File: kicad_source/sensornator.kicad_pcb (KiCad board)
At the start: 2 copper layers, 78 x 53 mm, 63 parts, among them CN1 ARDUINO, CON1 Micro_SDCard, P1 USB_OTG, Q1 2N7002, Q2 2N7002, Q3 BC847, Q4 BC847, Q5 NTR4171P, SW1 TAST_VER, SW2 TAST_VER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

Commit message: added pull up on BOOT
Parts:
- removed G*** (x2): generationmake_logo, labels:generationmake_logo
- added R25: 10k, Resistor_SMD:R_0603_1608Metric, F.Cu at (81.9, 113.5)
- BT1: value Battery -> Keystone 1043
- C9: value 100n -> 10u
- F1: value F_Small -> SF-1206S050
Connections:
- CN1 pad 15: (no net) -> unconnected-(CN1-Pad15)
- CN1 pad 31: (no net) -> unconnected-(CN1-Pad31)
- CON1 pad 1: (no net) -> unconnected-(CON1-Pad1)
- CON1 pad 8: (no net) -> unconnected-(CON1-Pad8)
- P1 pad 4: (no net) -> unconnected-(P1-Pad4)
- P1 pad 6: GND -> unconnected-(P1-Pad6)
- SW3 pad 3: (no net) -> unconnected-(SW3-Pad3)
- U3 pad 4: (no net) -> unconnected-(U3-Pad4)
- U4 pad 1: (no net) -> unconnected-(U4-Pad1)
- U4 pad 10: (no net) -> unconnected-(U4-Pad10)
- U4 pad 11: (no net) -> unconnected-(U4-Pad11)
- U4 pad 12: (no net) -> unconnected-(U4-Pad12)
- U4 pad 14: (no net) -> unconnected-(U4-Pad14)
- U4 pad 16: (no net) -> unconnected-(U4-Pad16)
- U4 pad 17: (no net) -> unconnected-(U4-Pad17)
- U4 pad 2: (no net) -> unconnected-(U4-Pad2)
- U4 pad 20: (no net) -> unconnected-(U4-Pad20)
- U4 pad 21: (no net) -> unconnected-(U4-Pad21)
- U4 pad 22: (no net) -> unconnected-(U4-Pad22)
- U4 pad 23: (no net) -> unconnected-(U4-Pad23)
- U4 pad 27: (no net) -> unconnected-(U4-Pad27)
- U5 pad 17: (no net) -> unconnected-(U5-Pad17)
- U5 pad 18: (no net) -> unconnected-(U5-Pad18)
- U5 pad 19: (no net) -> unconnected-(U5-Pad19)
- U5 pad 20: (no net) -> unconnected-(U5-Pad20)
- U5 pad 21: (no net) -> unconnected-(U5-Pad21)
- U5 pad 22: (no net) -> unconnected-(U5-Pad22)
- U5 pad 32: (no net) -> unconnected-(U5-Pad32)
- U6 pad 1: (no net) -> unconnected-(U6-Pad1)
- U6 pad 2: (no net) -> unconnected-(U6-Pad2)
- U6 pad 3: (no net) -> unconnected-(U6-Pad3)
- U6 pad 7: (no net) -> unconnected-(U6-Pad7)
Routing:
- net unconnected-(P1-Pad6): track 0.00 -> 8.00 mm
- net BOOT: track 42.1 -> 46.5 mm
- net +3V3: track 202.5 -> 205.4 mm
- net unconnected-(CON1-Pad1): track 0.00 -> 1.57 mm
- net (no net): track 1.57 -> 0.00 mm
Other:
- net class ANTENNA removed
- net class Default removed
- board text added: "1.2"
- board text removed: "1.1"

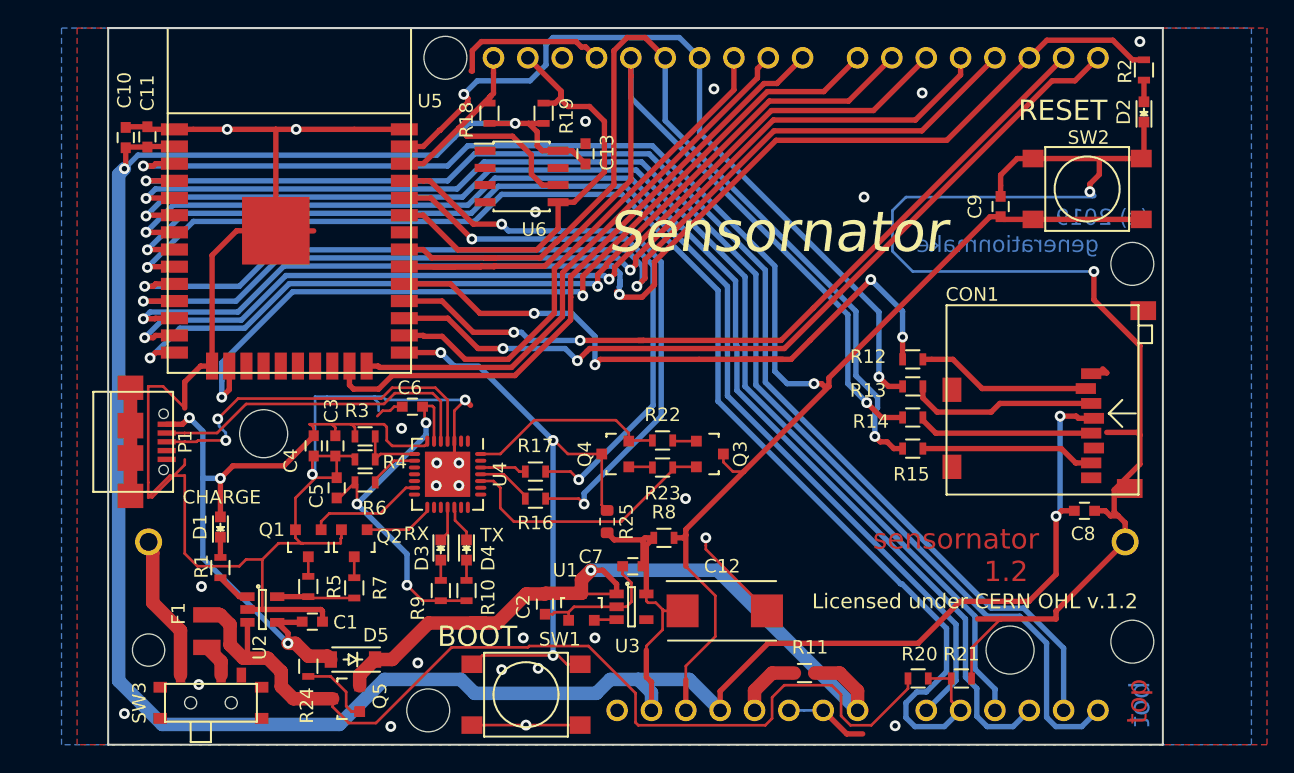
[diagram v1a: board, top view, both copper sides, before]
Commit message: added qwiic connector
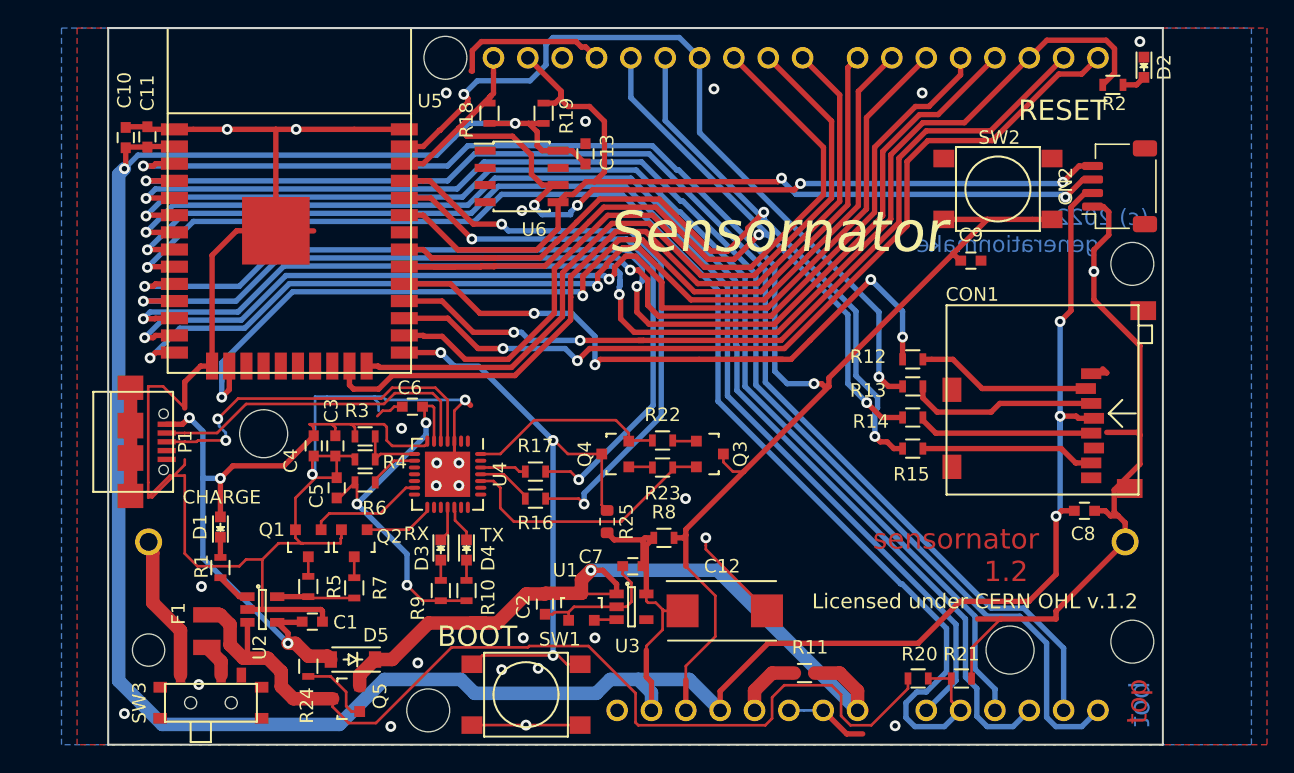
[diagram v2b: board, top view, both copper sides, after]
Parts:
- added CN2: SM04B-SRSS-TB, Connector_JST:JST_SH_SM04B-SRSS-TB_1x04-1MP_P1.00mm_Horizontal, F.Cu at (119.8, 88.7)
- moved SW2 6.60 mm to (110.8, 88.9)
- moved C9 4.57 mm to (108.8, 94.2), turned to 0 degrees
- moved D2 3.30 mm to (121.6, 79.9), turned to -90 degrees
- moved R2 2.55 mm to (119.3, 81.2), turned to 180 degrees
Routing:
- net GND: track 290.7 -> 244.6 mm, vias 29 -> 28
- net /I2C_SCL: track 21.9 -> 67.6 mm, vias 0 -> 4
- net /I2C_SDA: track 32.9 -> 71.0 mm, vias 0 -> 2
- net +3V3: track 205.4 -> 224.1 mm, vias 4 -> 5
- net /SPI_CS_EXT: track 37.7 -> 54.8 mm
- net /ARDUINO_9: track 41.5 -> 57.0 mm
- net /ARDUINO_8: track 47.0 -> 60.3 mm
- net /ARDUINO_7: track 62.5 -> 71.7 mm
- net /ARDUINO_5: track 69.1 -> 77.4 mm
- net /ARDUINO_6: track 66.8 -> 74.9 mm
- net /DAC_2: track 72.0 -> 78.4 mm
- net /DAC_1: track 76.6 -> 82.1 mm
- net /ARDUINO_2: track 89.9 -> 95.0 mm
- net /EXT_RX: track 61.9 -> 64.7 mm
- net /EXT_TX: track 63.3 -> 66.1 mm
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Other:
- board text added: "(c) 2022"
- board text removed: "(c) 2019"

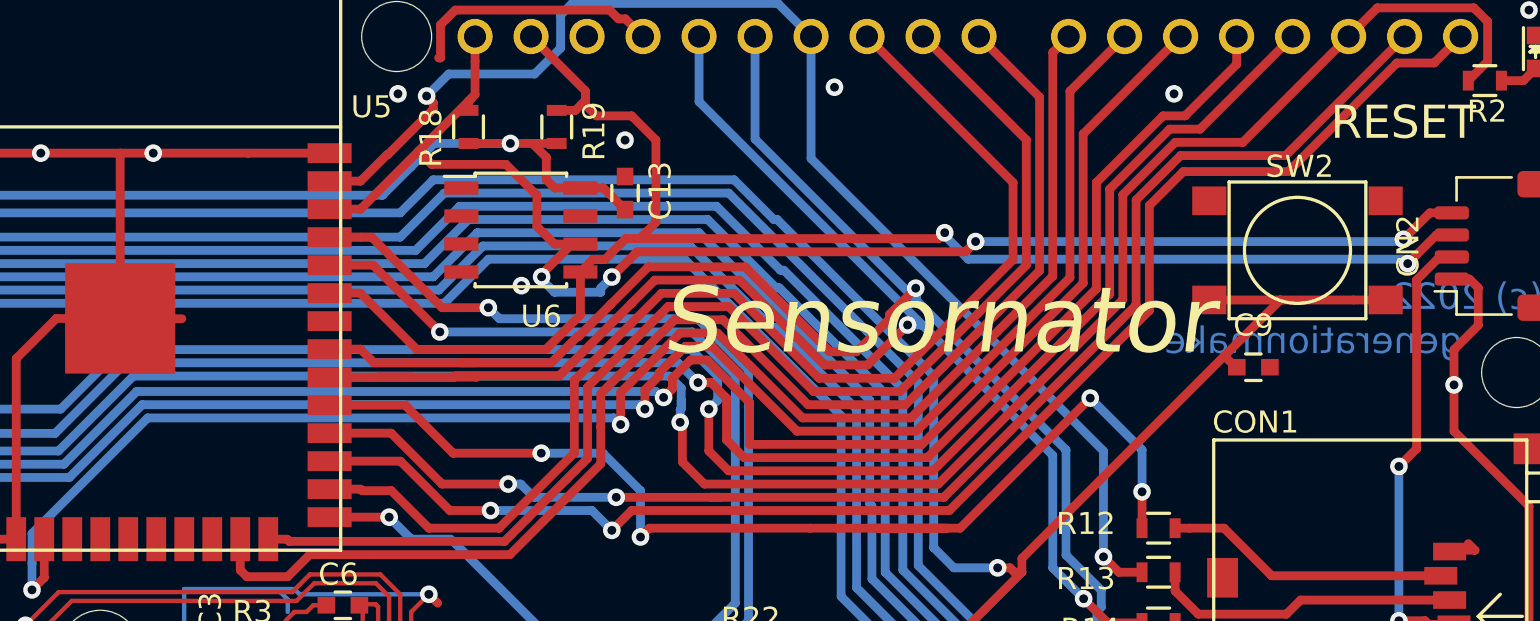
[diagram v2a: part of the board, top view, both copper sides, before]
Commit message: added i2c eeprom
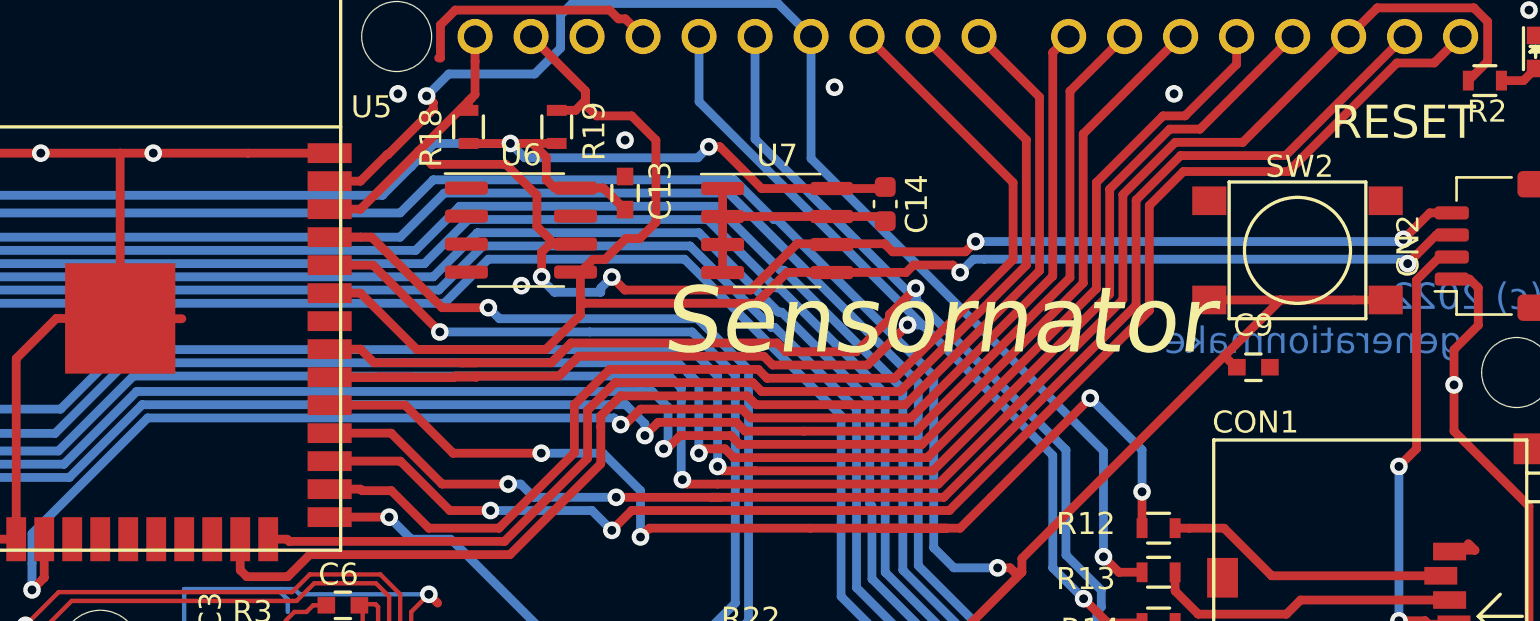
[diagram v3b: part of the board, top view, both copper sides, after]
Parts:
- added C14: 100n, Capacitor_SMD:C_0603_1608Metric, F.Cu at (92.1, 86.8)
- added U7: 24LC64, Package_SO:SOIC-8_3.9x4.9mm_P1.27mm, F.Cu at (87.2, 88.0)
- U6: footprint SOIC:SOIC-8_3.9x4.9mm_Pitch1.27mm -> Package_SO:SOIC-8_3.9x4.9mm_P1.27mm
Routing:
- net +3V3: track 224.1 -> 242.4 mm, vias 5 -> 6
- net GND: track 244.6 -> 255.9 mm
- net /ARDUINO_7: track 71.7 -> 68.0 mm
- net /SPI_CS_EXT: track 54.8 -> 51.3 mm
- net /ARDUINO_9: track 57.0 -> 53.5 mm
- net /ARDUINO_8: track 60.3 -> 56.9 mm
- net /I2C_SDA: track 71.0 -> 74.4 mm
- net /SPI_MISO: track 69.8 -> 67.0 mm
- net /SPI_CLK: track 75.2 -> 72.3 mm
- net /ARDUINO_6: track 74.9 -> 72.8 mm
- net /I2C_SCL: track 67.6 -> 69.3 mm
- net /DAC_2: track 78.4 -> 80.0 mm
- net /ARDUINO_5: track 77.4 -> 76.5 mm

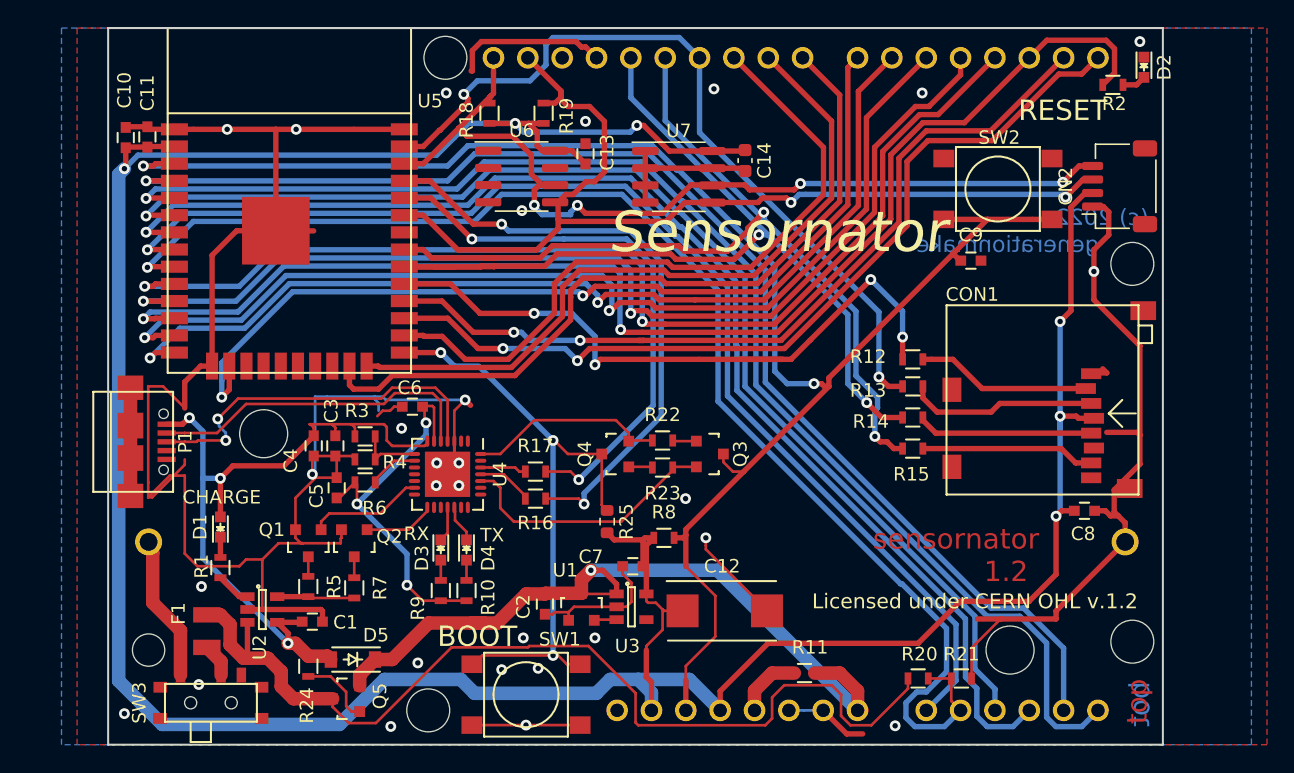
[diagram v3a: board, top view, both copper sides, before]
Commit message: updated footprint libraries
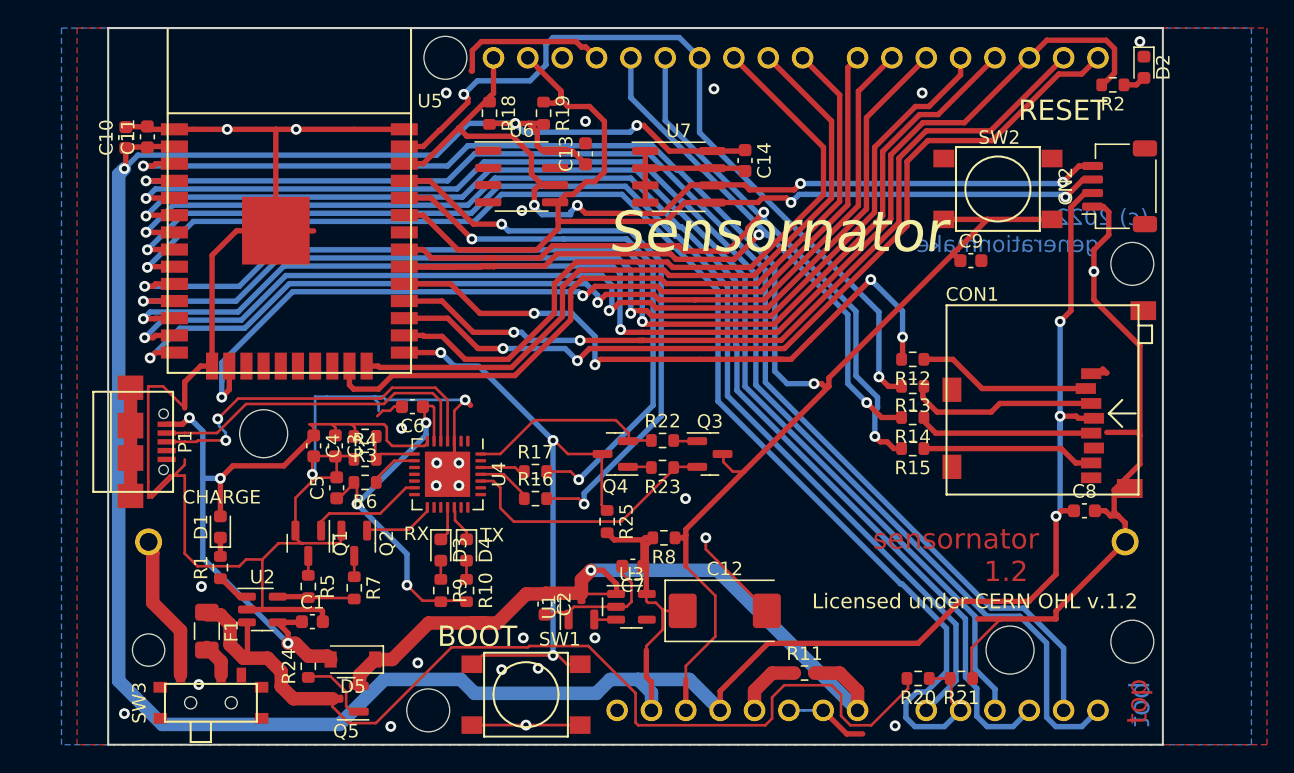
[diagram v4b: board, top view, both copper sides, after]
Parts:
- C1, C10, C11, C13, C2, C3, C4, C5, C6, C7, C8, C9: footprint capacitors:C_0603 -> Capacitor_SMD:C_0603_1608Metric
- C12: footprint capacitors:TantalC_SizeD_EIA-7343_Reflow -> Capacitor_Tantalum_SMD:CP_EIA-7343-31_Kemet-D
- D1, D2, D3, D4: footprint LEDs:LED_0603 -> LED_SMD:LED_0603_1608Metric
- D5: footprint diodes:SOD-123 -> Diode_SMD:D_SOD-123
- F1: footprint fuse_holders_and_fuses:Fuse_SMD1206_Reflow -> Fuse:Fuse_1206_3216Metric
- Q1, Q2, Q3, Q4, Q5, U1: footprint SOT_TO:SOT-23 -> Package_TO_SOT_SMD:SOT-23
- R1, R10, R11, R12, R13, R14, R15, R16, R17, R18, R19, R2, R20, R21, R22, R23, R24, R3, R4, R5, R6, R7, R8, R9: footprint resistors:R_0603 -> Resistor_SMD:R_0603_1608Metric
- U2, U3: footprint SOT_TO:SOT-23-5 -> Package_TO_SOT_SMD:SOT-23-5
- U4: footprint QFN:QFN-28-1EP_5x5mm_Pitch0.5mm -> Package_DFN_QFN:QFN-28-1EP_5x5mm_P0.5mm_EP3.35x3.35mm
- turned Q1 to -90 degrees
- turned Q2 to -90 degrees
- turned Q3 to 0 degrees
- turned Q4 to 180 degrees
- turned Q5 to 180 degrees
- turned U1 to 90 degrees

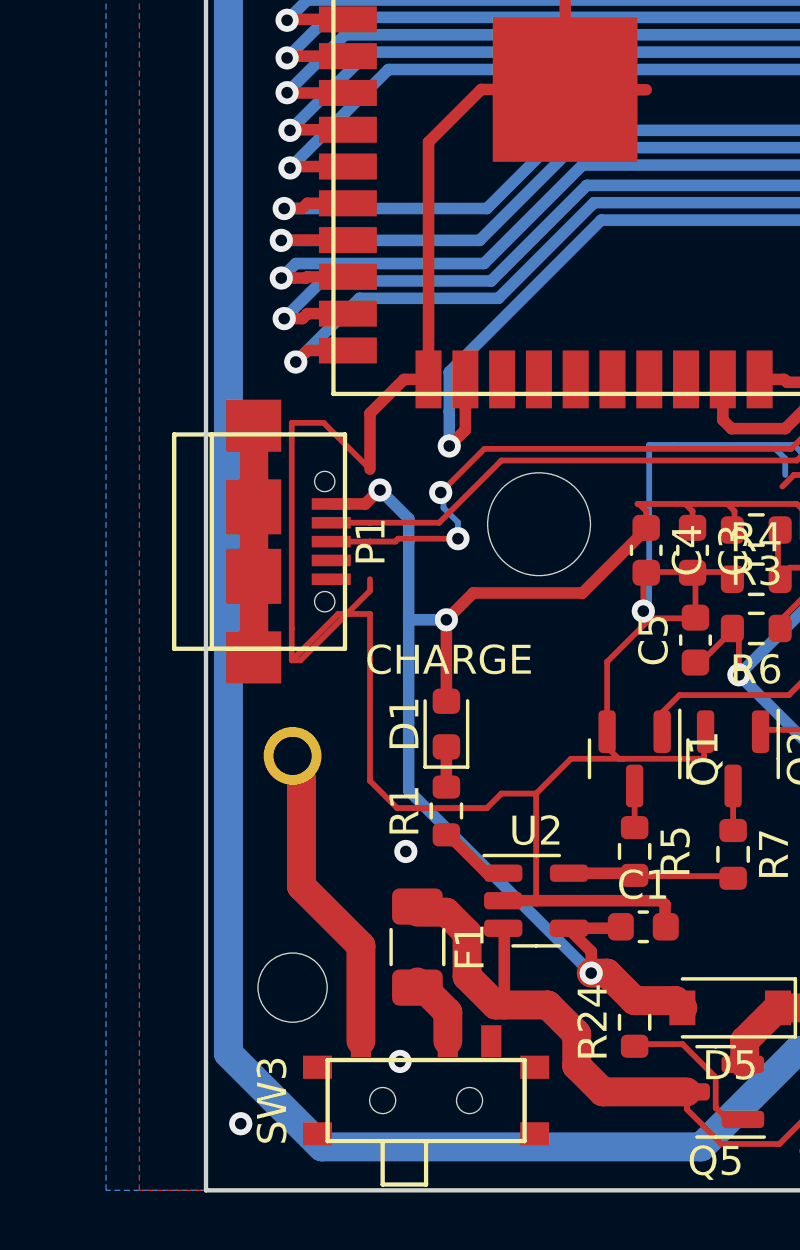
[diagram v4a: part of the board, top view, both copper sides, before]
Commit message: added CAN transceiver
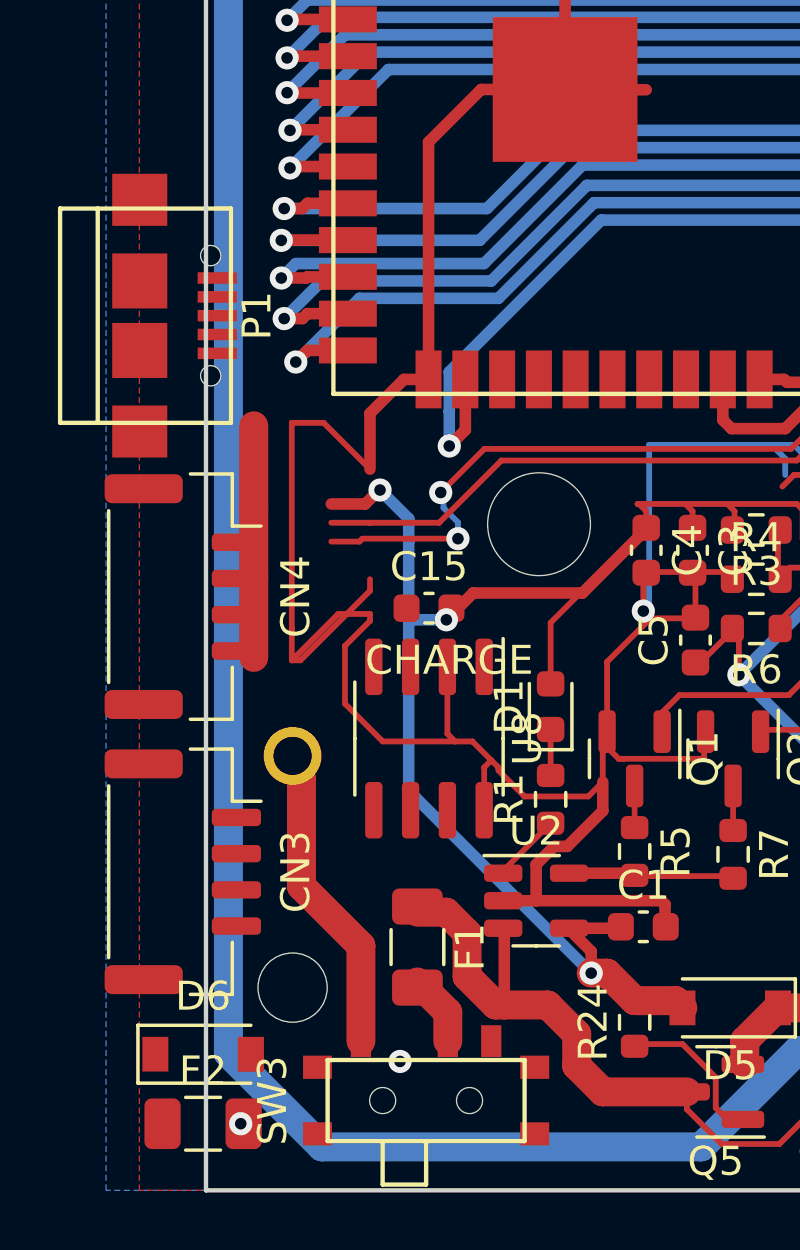
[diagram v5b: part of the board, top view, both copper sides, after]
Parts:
- added C15: 100n, Capacitor_SMD:C_0603_1608Metric, F.Cu at (52.7, 109.9)
- added CN3: SM04B-GHS-TB, Connector_JST:JST_GH_SM04B-GHS-TB_1x04-1MP_P1.25mm_Horizontal, F.Cu at (44.2, 119.0)
- added CN4: SM04B-GHS-TB, Connector_JST:JST_GH_SM04B-GHS-TB_1x04-1MP_P1.25mm_Horizontal, F.Cu at (44.2, 109.5)
- added D6: MBR120, Diode_SMD:D_SOD-123, F.Cu at (44.9, 125.3)
- added F2: SF-1206S050, Fuse:Fuse_1206_3216Metric, F.Cu at (44.9, 127.7)
- added U8: SN65HVD230, Package_SO:SOIC-8_3.9x4.9mm_P1.27mm, F.Cu at (52.7, 114.4)
- moved P1 8.74 mm to (46.1, 99.8)
- moved D1 3.65 mm to (56.9, 113.3)
- moved R1 3.62 mm to (56.9, 116.5)
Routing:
- net GND: track 255.9 -> 262.2 mm, vias 28 -> 26
- net VIN: track 54.5 -> 55.2 mm
- net VCC: vias 1 -> 2
